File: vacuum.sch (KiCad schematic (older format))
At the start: 66 parts, among them J1 к БП, J10 геркон шибера 1, J11 запасной, J12 запасной, J2 нагрузка, J3 нагрузка, J4 геркон клапана 0, J5 нагрузка, J6 нагрузка, J7 к БП, J8 геркон клапана 1, J9 геркон шибера 0, Q1 IRF740, Q2 IRF740, Q3 IRF740, Q4 IRF740, SW1 Кнопка, SW2 Кнопка, SW3 Кнопка, SW4 Выключить автоматику, SW5 Кнопка, U1 PC817, U10 PC817, U2 PC817, U3 PC817, U4 PC817, U5 PC817, U6 PC817, U7 PC817, U8 PC817, U9 PC817

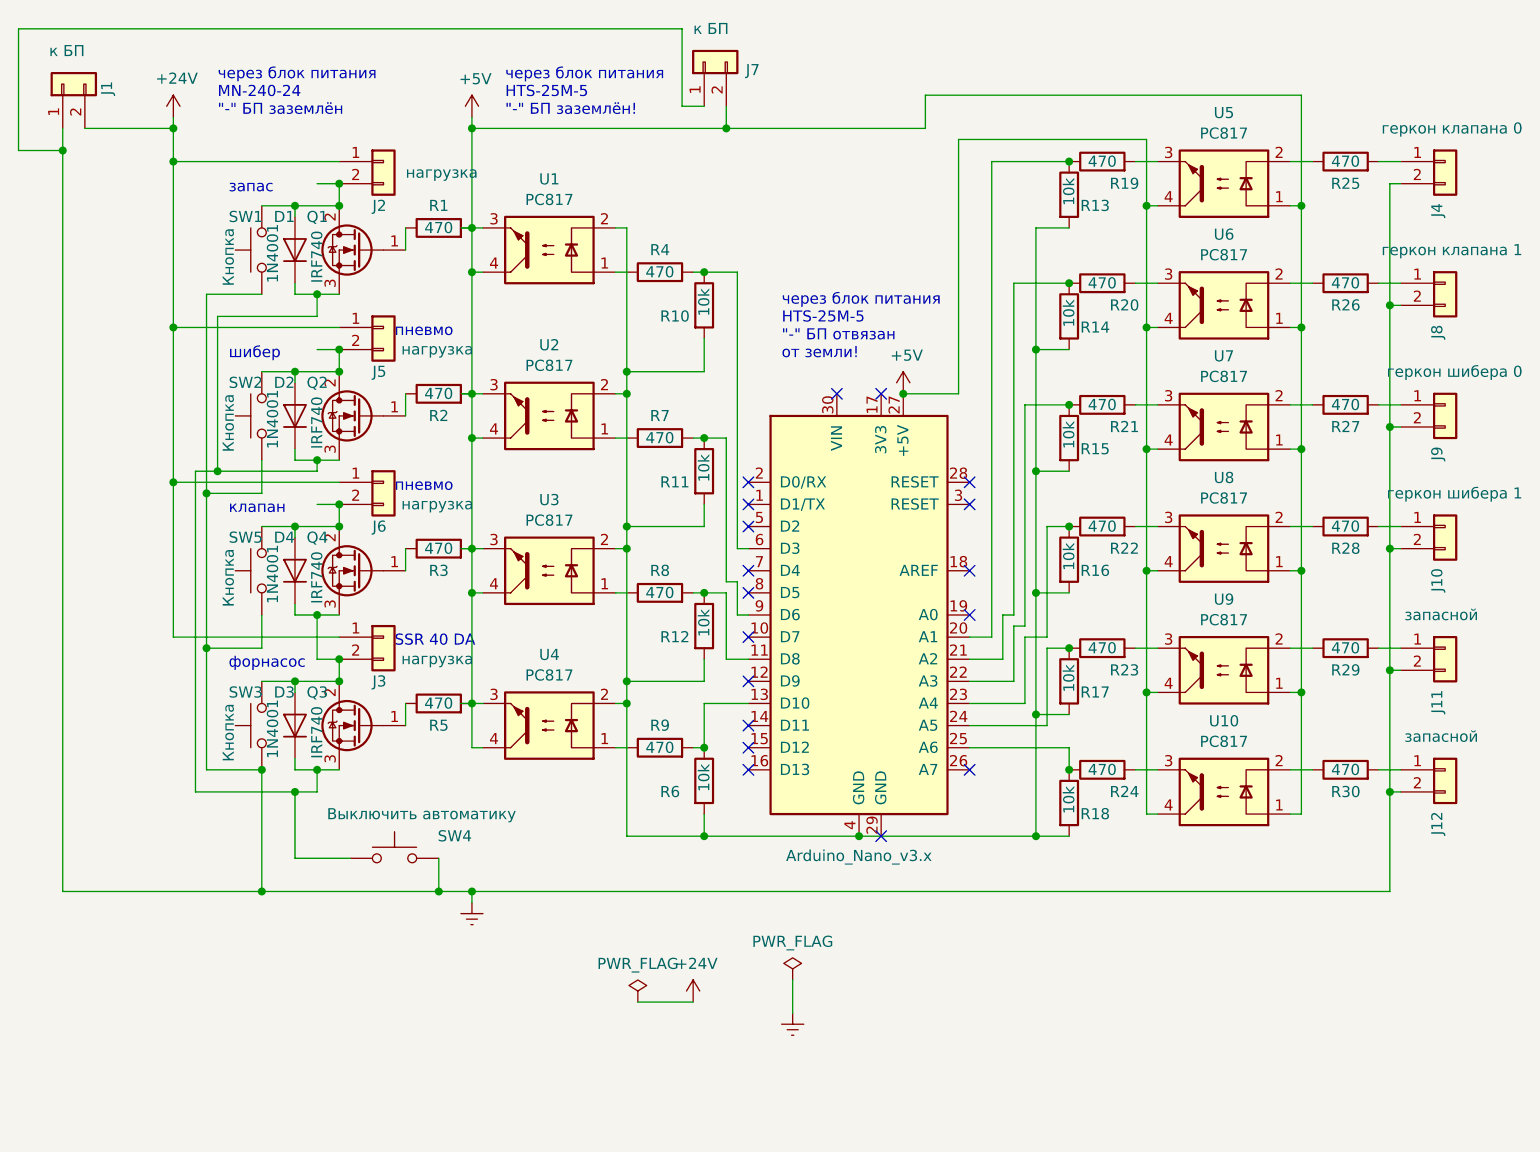
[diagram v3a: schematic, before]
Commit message: some connectors for power supply added
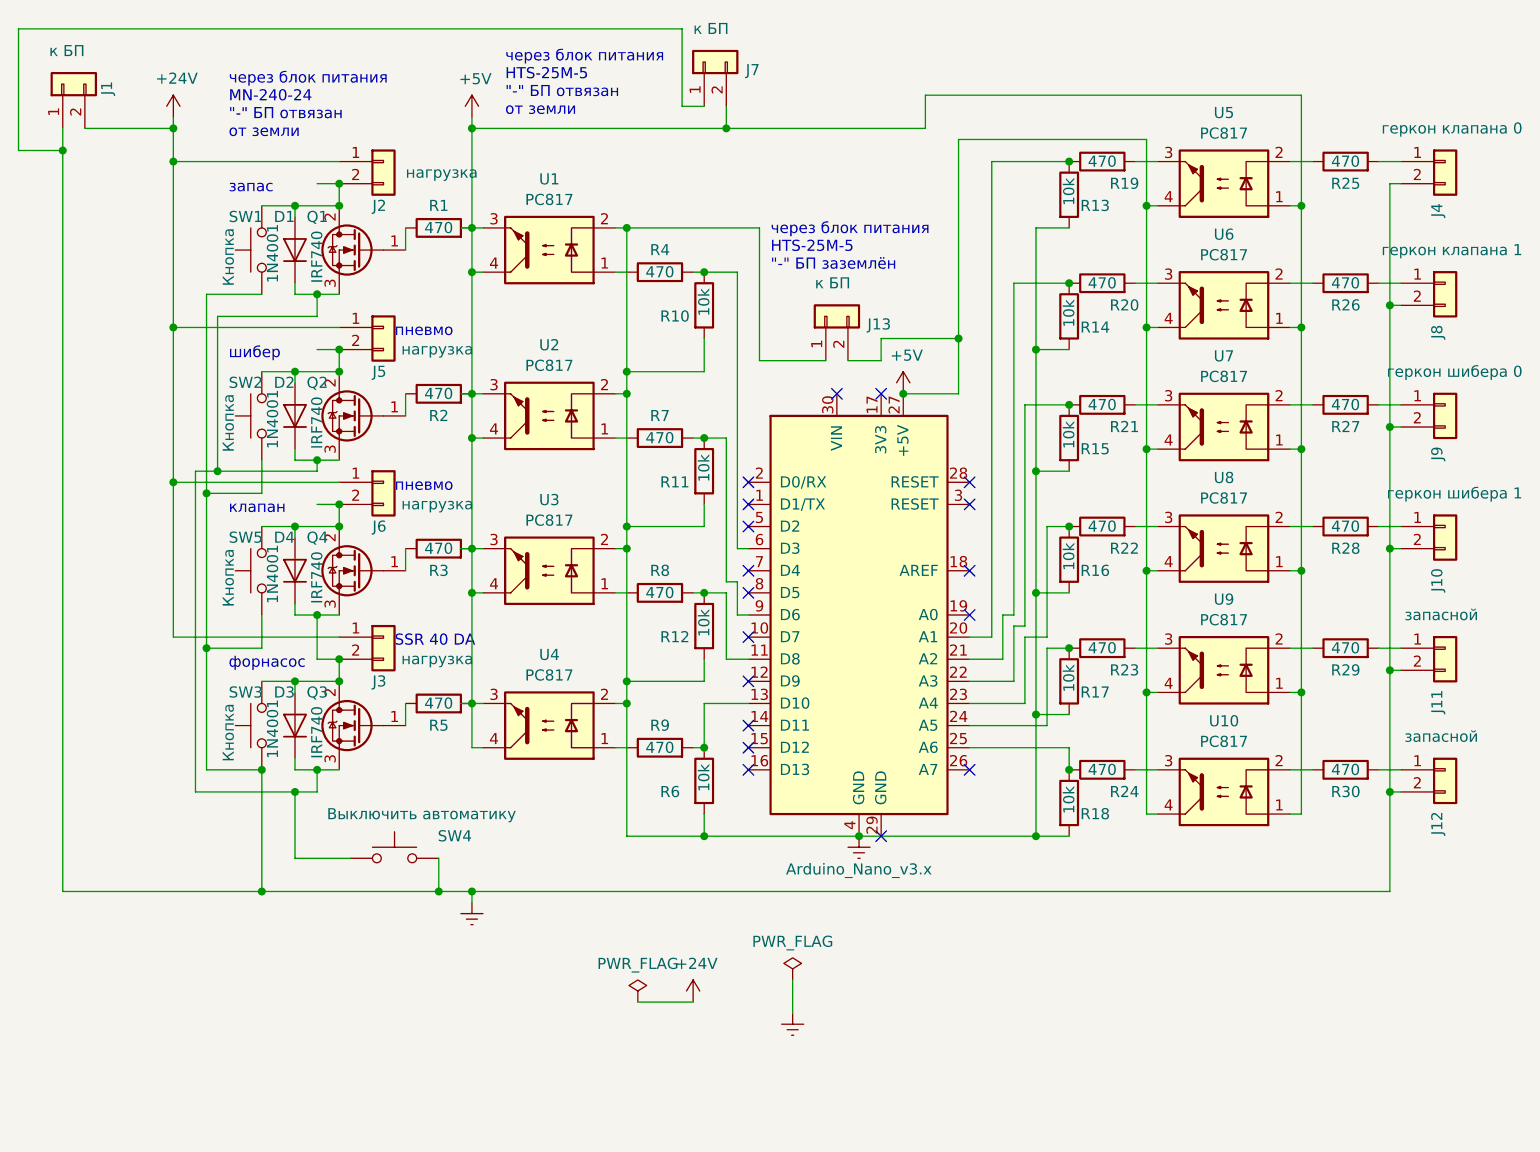
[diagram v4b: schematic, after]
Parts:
- added J13: к БП, Connector_Phoenix_MSTB:PhoenixContact_MSTBV_2,5_2-GF_1x02_P5.00mm_Vertical_ThreadedFlange, symbol Connector_Generic:Conn_01x02
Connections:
- wire segments 243 -> 250
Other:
- note added: "через блок питания \nHTS-25M-5\n"-" БП заземлён"
- note added: "через блок питания \nHTS-25M-5\n"-" БП отвязан\nот земли"
- note added: "через блок питания\nMN-240-24\n"-" БП отвязан\nот земли"
- note removed: "через блок питания \nHTS-25M-5\n"-" БП заземлён!"
- note removed: "через блок питания \nHTS-25M-5\n"-" БП отвязан \nот земли!"
- note removed: "через блок питания\nMN-240-24\n"-" БП заземлён"
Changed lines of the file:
@@
 	1    0    0    -1
 $EndComp
-Text Notes 2050 2850 0    50   ~ 0
-через блок питания\nMN-240-24\n"-" БП заземлён
 Connection ~ 3200 3550
 Wire Wire Line
@@
 	1    0    0    -1
 $EndComp
-Text Notes 3350 2850 0    50   ~ 0
-через блок питания \nHTS-25M-5\n"-" БП заземлён!
 $Comp
 L power:+5V #PWR05
@@
 	1    0    0    -1
 $EndComp
-Text Notes 4600 3950 0    50   ~ 0
-через блок питания \nHTS-25M-5\n"-" БП отвязан \nот земли!
 NoConn ~ 5450 4500
 NoConn ~ 5450 4600
@@
 P 4950 5100
 F 0 "A1" H 4950 4011 50  0001 C CNN
-F 1 "Arduino_Nano_v3.x" H 4950 4011 50  0000 C CNN
+F 1 "Arduino_Nano_v3.x" H 4950 3950 50  0000 C CNN
 F 2 "Module:Arduino_Nano" H 5100 4150 50  0001 L CNN
 F 3 "http://www.mouser.com/pdfdocs/Gravitech_Arduino_Nano3_0.pdf" H 4950 4100 50  0001 C CNN
@@
 	6250 2950 5400 2950
 Wire Wire Line
-	5400 2950 5400 4100
+	5400 2950 5400 3850
 Wire Wire Line
 	5400 4100 5150 4100
@@
 	1350 3000 1350 6350
 NoConn ~ 5450 5100
+Text Notes 4550 3550 0    50   ~ 0
+через блок питания \nHTS-25M-5\n"-" БП заземлён
+Text Notes 2100 2950 0    50   ~ 0
+через блок питания\nMN-240-24\n"-" БП отвязан\nот земли
+Text Notes 3350 2850 0    50   ~ 0
+через блок питания \nHTS-25M-5\n"-" БП отвязан\nот земли
+$Comp
+L Connector_Generic:Conn_01x02 J13
+U 1 1 5D3377BE
+P 4800 3750
+F 0 "J13" V 4764 3562 50  0000 R CNN
+F 1 "к БП" V 4950 3800 50  0000 R CNN
+F 2 "Connector_Phoenix_MSTB:PhoenixContact_MSTBV_2,5_2-GF_1x02_P5.00mm_Vertical_ThreadedFlange" H 4800 3750 50  0001 C CNN
+F 3 "~" H 4800 3750 50  0001 C CNN
+	1    4800 3750
+	0    -1   -1   0
+$EndComp
+Wire Wire Line
+	4900 3950 5050 3950
+Wire Wire Line
+	5050 3950 5050 3850
+Wire Wire Line
+	5050 3850 5400 3850
+Connection ~ 5400 3850
+Wire Wire Line
+	5400 3850 5400 4100
+Wire Wire Line
+	4500 3950 4500 3350
+Wire Wire Line
+	4500 3350 3900 3350
+Connection ~ 3900 3350
+Wire Wire Line
+	4500 3950 4800 3950
+$Comp
+L power:Earth #PWR0102
+U 1 1 5D3943C7
+P 4950 6100
+F 0 "#PWR0102" H 4950 5850 50  0001 C CNN
+F 1 "Earth" H 4950 5950 50  0001 C CNN
+F 2 "" H 4950 6100 50  0001 C CNN
+F 3 "~" H 4950 6100 50  0001 C CNN
+	1    4950 6100
+	1    0    0    -1
+$EndComp
 $EndSCHEMATC

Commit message: some scheme bags removed
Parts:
- A1: value Arduino_Nano_v3.x -> Arduino_Nano_v3; footprint Module:Arduino_Nano -> Module:Arduino_Nano_WithMountingHoles
- J1, J10, J11, J12, J13, J2, J3, J4, J5, J6, J7, J8, J9: footprint Connector_Phoenix_MSTB:PhoenixContact_MSTBV_2,5_2-GF_1x02_P5.00mm_Vertical_ThreadedFlange -> TerminalBlock_Altech:Altech_AK300_1x02_P5.00mm_45-Degree
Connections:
- wire segments 250 -> 249
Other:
- note added: "запасной"
- note removed: "запас"
- moved on the sheet: J1
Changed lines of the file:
@@
 L power:Earth #PWR03
 U 1 1 5D280DBC
-P 3200 6400
-F 0 "#PWR03" H 3200 6150 50  0001 C CNN
-F 1 "Earth" H 3200 6250 50  0001 C CNN
-F 2 "" H 3200 6400 50  0001 C CNN
-F 3 "~" H 3200 6400 50  0001 C CNN
-	1    3200 6400
+P 3550 6200
+F 0 "#PWR03" H 3550 5950 50  0001 C CNN
+F 1 "Earth" H 3550 6050 50  0001 C CNN
+F 2 "" H 3550 6200 50  0001 C CNN
+F 3 "~" H 3550 6200 50  0001 C CNN
+	1    3550 6200
 	1    0    0    -1
 $EndComp
@@
 F 0 "J3" H 2750 5000 50  0000 L CNN
 F 1 "нагрузка" H 2880 5101 50  0000 L CNN
-F 2 "Connector_Phoenix_MSTB:PhoenixContact_MSTBV_2,5_2-GF_1x02_P5.00mm_Vertical_ThreadedFlange" H 2800 5200 50  0001 C CNN
+F 2 "TerminalBlock_Altech:Altech_AK300_1x02_P5.00mm_45-Degree" H 2800 5200 50  0001 C CNN
 F 3 "~" H 2800 5200 50  0001 C CNN
 	1    2800 5200
@@
 NoConn ~ 5050 6100
 Wire Wire Line
-	3200 6400 3200 6350
+	3550 6200 3550 6150
 $Comp
 L power:Earth #PWR0101
@@
 F 0 "J6" H 2750 4300 50  0000 L CNN
 F 1 "нагрузка" H 2880 4401 50  0000 L CNN
-F 2 "Connector_Phoenix_MSTB:PhoenixContact_MSTBV_2,5_2-GF_1x02_P5.00mm_Vertical_ThreadedFlange" H 2800 4500 50  0001 C CNN
+F 2 "TerminalBlock_Altech:Altech_AK300_1x02_P5.00mm_45-Degree" H 2800 4500 50  0001 C CNN
 F 3 "~" H 2800 4500 50  0001 C CNN
 	1    2800 4500
@@
 Text Notes 2850 4550 0    50   ~ 0
 пневмо
-Wire Wire Line
-	2600 4600 2500 4600
-Connection ~ 2600 4600
 $Comp
 L Isolator:PC817 U3
@@
 F 0 "J5" H 2750 3600 50  0000 L CNN
 F 1 "нагрузка" H 2880 3701 50  0000 L CNN
-F 2 "Connector_Phoenix_MSTB:PhoenixContact_MSTBV_2,5_2-GF_1x02_P5.00mm_Vertical_ThreadedFlange" H 2800 3800 50  0001 C CNN
+F 2 "TerminalBlock_Altech:Altech_AK300_1x02_P5.00mm_45-Degree" H 2800 3800 50  0001 C CNN
 F 3 "~" H 2800 3800 50  0001 C CNN
 	1    2800 3800
@@
 Text Notes 2850 3850 0    50   ~ 0
 пневмо
-Wire Wire Line
-	2600 3900 2500 3900
-Connection ~ 2600 3900
 $Comp
 L Isolator:PC817 U2
@@
 	2600 3250 2600 3150
 Text Notes 2100 3200 0    50   ~ 0
-запас
+запасной
 $Comp
 L Connector_Generic:Conn_01x02 J2
@@
 F 0 "J2" H 2750 2850 50  0000 L CNN
 F 1 "нагрузка" H 2900 3000 50  0000 L CNN
-F 2 "Connector_Phoenix_MSTB:PhoenixContact_MSTBV_2,5_2-GF_1x02_P5.00mm_Vertical_ThreadedFlange" H 2800 3050 50  0001 C CNN
+F 2 "TerminalBlock_Altech:Altech_AK300_1x02_P5.00mm_45-Degree" H 2800 3050 50  0001 C CNN
 F 3 "~" H 2800 3050 50  0001 C CNN
 	1    2800 3050
@@
 	1    0    0    -1
 $EndComp
-Wire Wire Line
-	2600 3150 2500 3150
-Connection ~ 2600 3150
 $Comp
 L Isolator:PC817 U1
@@
 	4400 4800 4450 4800
 Connection ~ 3050 6350
-Wire Wire Line
-	1850 2850 1850 2900
 Connection ~ 1850 3050
 Wire Wire Line
@@
 	3200 5500 3200 5000
 Wire Wire Line
-	3200 6350 3050 6350
-Wire Wire Line
 	2250 5800 2250 6350
 $Comp
@@
 P 4950 5100
 F 0 "A1" H 4950 4011 50  0001 C CNN
-F 1 "Arduino_Nano_v3.x" H 4950 3950 50  0000 C CNN
-F 2 "Module:Arduino_Nano" H 5100 4150 50  0001 L CNN
+F 1 "Arduino_Nano_v3" H 4950 3950 50  0000 C CNN
+F 2 "Module:Arduino_Nano_WithMountingHoles" H 5100 4150 50  0001 L CNN
 F 3 "http://www.mouser.com/pdfdocs/Gravitech_Arduino_Nano3_0.pdf" H 4950 4100 50  0001 C CNN
 	1    4950 5100
@@
 Wire Wire Line
 	3200 2900 3200 2850
-Connection ~ 3200 6350
 $Comp
 L Device:R R25
@@
 F 0 "J12" V 7564 5612 50  0000 R CNN
 F 1 "запасной" H 7750 5950 50  0000 R CNN
-F 2 "Connector_Phoenix_MSTB:PhoenixContact_MSTBV_2,5_2-GF_1x02_P5.00mm_Vertical_ThreadedFlange" H 7600 5800 50  0001 C CNN
+F 2 "TerminalBlock_Altech:Altech_AK300_1x02_P5.00mm_45-Degree" H 7600 5800 50  0001 C CNN
 F 3 "~" H 7600 5800 50  0001 C CNN
 	1    7600 5800
@@
 F 0 "J11" V 7564 5062 50  0000 R CNN
 F 1 "запасной" H 7750 5400 50  0000 R CNN
-F 2 "Connector_Phoenix_MSTB:PhoenixContact_MSTBV_2,5_2-GF_1x02_P5.00mm_Vertical_ThreadedFlange" H 7600 5250 50  0001 C CNN
+F 2 "TerminalBlock_Altech:Altech_AK300_1x02_P5.00mm_45-Degree" H 7600 5250 50  0001 C CNN
 F 3 "~" H 7600 5250 50  0001 C CNN
 	1    7600 5250
@@
 P 7600 4700
 F 0 "J10" V 7564 4512 50  0000 R CNN
-F 1 "геркон шибера 1" H 7950 4850 50  0000 R CNN
-F 2 "Connector_Phoenix_MSTB:PhoenixContact_MSTBV_2,5_2-GF_1x02_P5.00mm_Vertical_ThreadedFlange" H 7600 4700 50  0001 C CNN
+F 1 "геркон шибера 1" H 7700 4850 50  0000 R CNN
+F 2 "TerminalBlock_Altech:Altech_AK300_1x02_P5.00mm_45-Degree" H 7600 4700 50  0001 C CNN
 F 3 "~" H 7600 4700 50  0001 C CNN
 	1    7600 4700
@@
 P 7600 4150
 F 0 "J9" V 7564 3962 50  0000 R CNN
-F 1 "геркон шибера 0" H 7950 4300 50  0000 R CNN
-F 2 "Connector_Phoenix_MSTB:PhoenixContact_MSTBV_2,5_2-GF_1x02_P5.00mm_Vertical_ThreadedFlange" H 7600 4150 50  0001 C CNN
+F 1 "геркон шибера 0" H 7700 4300 50  0000 R CNN
+F 2 "TerminalBlock_Altech:Altech_AK300_1x02_P5.00mm_45-Degree" H 7600 4150 50  0001 C CNN
 F 3 "~" H 7600 4150 50  0001 C CNN
 	1    7600 4150
@@
 P 7600 3600
 F 0 "J8" V 7564 3412 50  0000 R CNN
-F 1 "геркон клапана 1" H 7950 3750 50  0000 R CNN
-F 2 "Connector_Phoenix_MSTB:PhoenixContact_MSTBV_2,5_2-GF_1x02_P5.00mm_Vertical_ThreadedFlange" H 7600 3600 50  0001 C CNN
+F 1 "геркон клапана 1" H 7700 3750 50  0000 R CNN
+F 2 "TerminalBlock_Altech:Altech_AK300_1x02_P5.00mm_45-Degree" H 7600 3600 50  0001 C CNN
 F 3 "~" H 7600 3600 50  0001 C CNN
 	1    7600 3600
@@
 P 7600 3050
 F 0 "J4" V 7564 2862 50  0000 R CNN
-F 1 "геркон клапана 0" H 7950 3200 50  0000 R CNN
-F 2 "Connector_Phoenix_MSTB:PhoenixContact_MSTBV_2,5_2-GF_1x02_P5.00mm_Vertical_ThreadedFlange" H 7600 3050 50  0001 C CNN
+F 1 "геркон клапана 0" H 7700 3200 50  0000 R CNN
+F 2 "TerminalBlock_Altech:Altech_AK300_1x02_P5.00mm_45-Degree" H 7600 3050 50  0001 C CNN
 F 3 "~" H 7600 3050 50  0001 C CNN
 	1    7600 3050
@@
 $EndComp
 Wire Wire Line
-	7350 6350 3200 6350
-Wire Wire Line
 	6900 3050 7000 3050
 Wire Wire Line
@@
 L Connector_Generic:Conn_01x02 J1
 U 1 1 5DDC5F15
-P 1350 2700
-F 0 "J1" H 1300 2500 50  0000 L CNN
-F 1 "к БП" V 1500 2600 50  0000 L CNN
-F 2 "Connector_Phoenix_MSTB:PhoenixContact_MSTBV_2,5_2-GF_1x02_P5.00mm_Vertical_ThreadedFlange" H 1350 2700 50  0001 C CNN
-F 3 "~" H 1350 2700 50  0001 C CNN
-	1    1350 2700
-	0    -1   -1   0
-$EndComp
-Wire Wire Line
-	1450 2900 1850 2900
-Connection ~ 1850 2900
-Wire Wire Line
-	1850 2900 1850 3050
-Wire Wire Line
-	1350 2900 1350 3000
-Wire Wire Line
-	1350 6350 2250 6350
-Connection ~ 2250 6350
+P 2200 2750
+F 0 "J1" H 2150 2550 50  0000 L CNN
+F 1 "к БП" V 2350 2650 50  0000 L CNN
+F 2 "TerminalBlock_Altech:Altech_AK300_1x02_P5.00mm_45-Degree" H 2200 2750 50  0001 C CNN
+F 3 "~" H 2200 2750 50  0001 C CNN
+	1    2200 2750
+	0    1    -1   0
+$EndComp
 $Comp
 L Connector_Generic:Conn_01x02 J7
@@
 P 4250 2600
 F 0 "J7" V 4214 2412 50  0000 R CNN
-F 1 "к БП" V 4400 2650 50  0000 R CNN
-F 2 "Connector_Phoenix_MSTB:PhoenixContact_MSTBV_2,5_2-GF_1x02_P5.00mm_Vertical_ThreadedFlange" H 4250 2600 50  0001 C CNN
+F 1 "к БП" V 4100 2450 50  0000 R CNN
+F 2 "TerminalBlock_Altech:Altech_AK300_1x02_P5.00mm_45-Degree" H 4250 2600 50  0001 C CNN
 F 3 "~" H 4250 2600 50  0001 C CNN
 	1    4250 2600
@@
 	4250 2800 4150 2800
 Wire Wire Line
-	4150 2800 4150 2450
-Wire Wire Line
-	4150 2450 1150 2450
-Wire Wire Line
-	1150 2450 1150 3000
-Wire Wire Line
-	1150 3000 1350 3000
-Connection ~ 1350 3000
-Wire Wire Line
-	1350 3000 1350 6350
+	4150 2800 4150 2550
 NoConn ~ 5450 5100
 Text Notes 4550 3550 0    50   ~ 0
 через блок питания \nHTS-25M-5\n"-" БП заземлён
-Text Notes 2100 2950 0    50   ~ 0
+Text Notes 2350 2950 0    50   ~ 0
 через блок питания\nMN-240-24\n"-" БП отвязан\nот земли
-Text Notes 3350 2850 0    50   ~ 0
+Text Notes 3350 2900 0    50   ~ 0
 через блок питания \nHTS-25M-5\n"-" БП отвязан\nот земли
 $Comp
@@
 F 0 "J13" V 4764 3562 50  0000 R CNN
 F 1 "к БП" V 4950 3800 50  0000 R CNN
-F 2 "Connector_Phoenix_MSTB:PhoenixContact_MSTBV_2,5_2-GF_1x02_P5.00mm_Vertical_ThreadedFlange" H 4800 3750 50  0001 C CNN
+F 2 "TerminalBlock_Altech:Altech_AK300_1x02_P5.00mm_45-Degree" H 4800 3750 50  0001 C CNN
 F 3 "~" H 4800 3750 50  0001 C CNN
 	1    4800 3750
@@
 	1    0    0    -1
 $EndComp
+Wire Wire Line
+	1850 2850 1850 2950
+Wire Wire Line
+	2100 2950 1850 2950
+Connection ~ 1850 2950
+Wire Wire Line
+	1850 2950 1850 3050
+Wire Wire Line
+	2200 2950 2300 2950
+Wire Wire Line
+	2300 2950 2300 2550
+Wire Wire Line
+	2300 2550 1750 2550
+Wire Wire Line
+	1750 2550 1750 6350
+Wire Wire Line
+	1750 6350 2250 6350
+Connection ~ 2250 6350
+Wire Wire Line
+	2300 2550 4150 2550
+Connection ~ 2300 2550
+Wire Wire Line
+	3050 6350 3450 6350
+Wire Wire Line
+	3550 6150 3450 6150
+Wire Wire Line
+	3450 6150 3450 6350
+Connection ~ 3450 6350
+Wire Wire Line
+	3450 6350 7350 6350
 $EndSCHEMATC
